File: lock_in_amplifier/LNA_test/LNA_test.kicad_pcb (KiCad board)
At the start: 2 copper layers, 110 parts, among them J1 vref-in, J10 A IN, J11 B IN, J12 POWER_IN, J15 I IN, J17 RF_Shield_One_Piece, J19 +3V3 OUT, J2 vref, J20 AMP OUT, J3 V-IN, J38 RF_Shield_One_Piece, J4 GND, J46 -5V OUT, J47 +5V OUT, J5 V+IN, J6 +5V, J7 +3V3, J8 -5V, Q1 DMN640L, Q2 DMN640L, U1 LM833, U6 lmp7721, U7 LM833, U8 AD8429

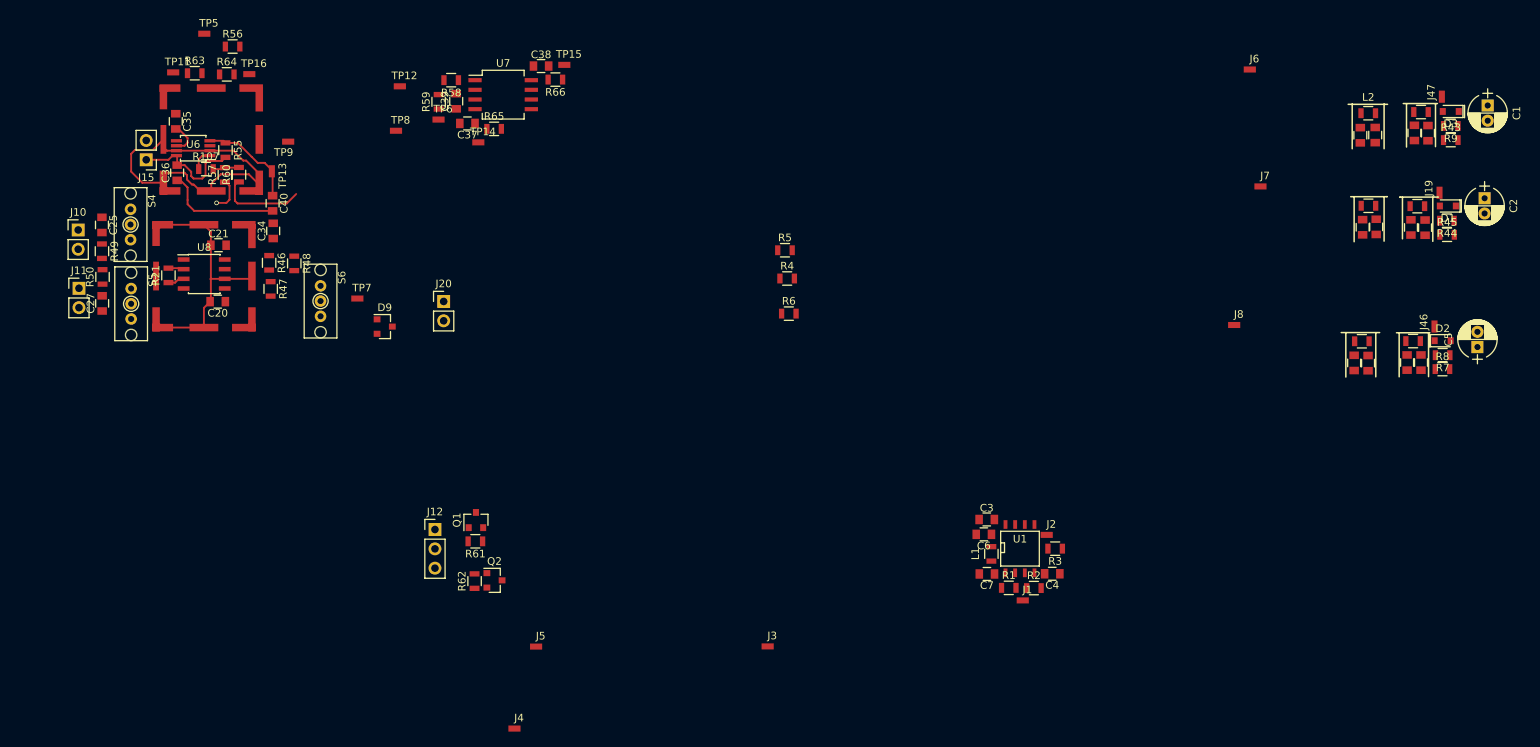
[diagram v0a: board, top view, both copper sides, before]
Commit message: initial lna and power floorplan finished.
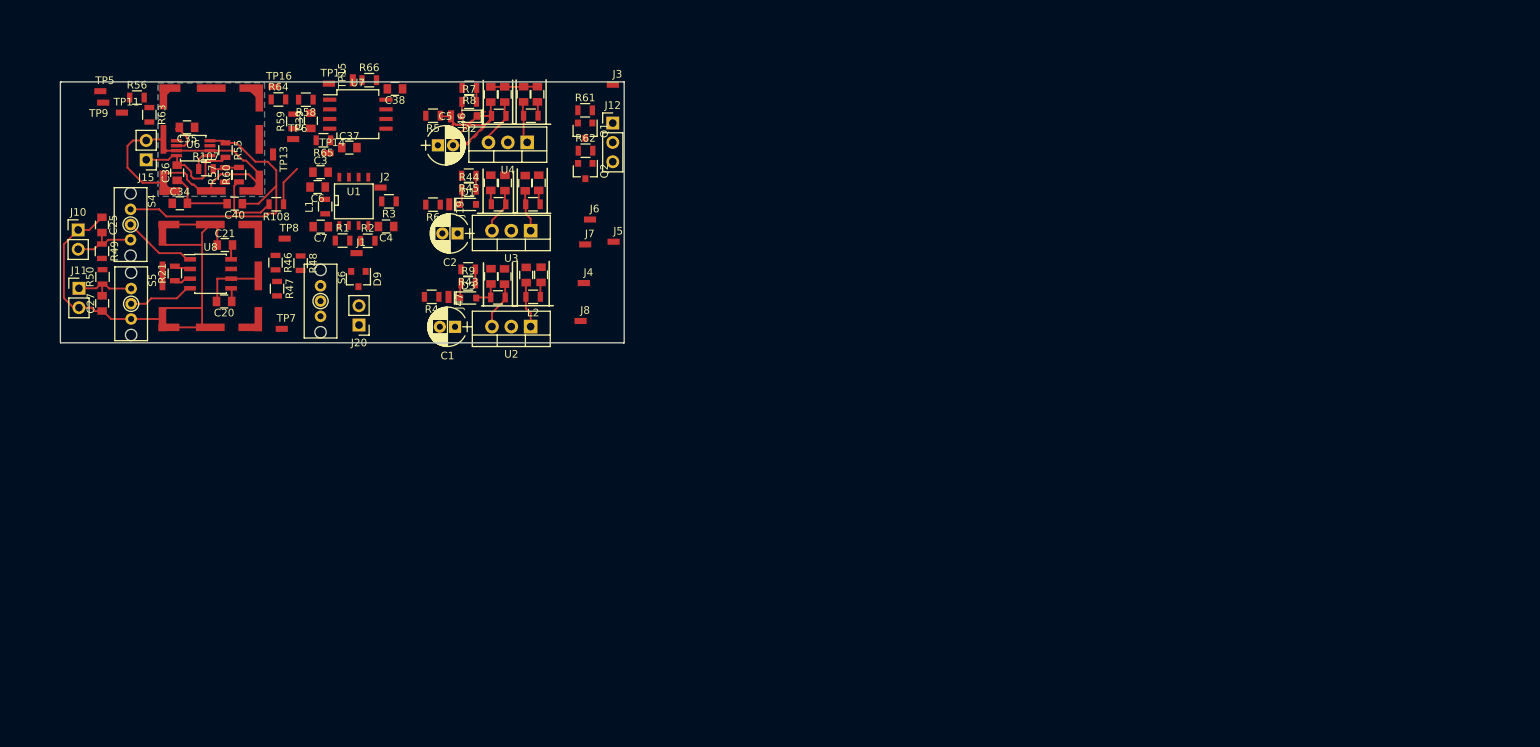
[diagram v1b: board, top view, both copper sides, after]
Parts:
- added R108: 0, Resistors_SMD:R_0805, F.Cu at (111.4, 79.3)
- added U2: lm7805, TO_SOT_Packages_THT:TO-220-3_Vertical, F.Cu at (144.8, 95.4)
- added U3: LM7833, TO_SOT_Packages_THT:TO-220-3_Vertical, F.Cu at (144.8, 82.8)
- added U4: lm7905, TO_SOT_Packages_THT:TO-220-3_Vertical, F.Cu at (144.3, 71.2)
- moved C5 139.2 mm to (132.6, 71.6), turned to 0 degrees
- moved C1 138.8 mm to (134.8, 95.4), turned to 180 degrees
- moved C2 135.1 mm to (135.2, 83.1), turned to 180 degrees
- moved R8 133.1 mm to (136.7, 64.0), turned to 180 degrees
- moved R7 132.2 mm to (136.7, 65.8), turned to 0 degrees
- moved D3 131.4 mm to (136.6, 91.6), turned to 0 degrees
- moved D2 131.3 mm to (136.7, 67.7), turned to 180 degrees
- moved R9 130.8 mm to (136.6, 89.7), turned to 0 degrees
- moved R43 130.2 mm to (136.6, 87.9), turned to 180 degrees
- moved J47 129.7 mm to (135.9, 92.1), turned to 270 degrees
- moved R45 128.8 mm to (136.7, 75.5), turned to 180 degrees
- moved D1 128.8 mm to (136.6, 79.3), turned to 0 degrees
- moved R44 128.6 mm to (136.7, 77.4), turned to 0 degrees
- moved J46 128.2 mm to (136.2, 68.4), turned to 270 degrees
- moved C17 127.2 mm to (139.5, 64.9), turned to 90 degrees
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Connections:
- J15 pad 2: GND -> /sheet5A330123/GUARD
- J17 pad 1: Net-(J17-Pad1) -> /sheet5A330123/GUARD
- Q1 pad 1: /sheet5A330121/V-_IN -> /sheet5A330121/GND_IN
- Q1 pad 2: /sheet5A330121/GND_IN -> Net-(C10-Pad1)
- Q1 pad 3: Net-(C10-Pad1) -> /sheet5A330121/V-_IN
- Q2 pad 1: /sheet5A330121/GND_IN -> /sheet5A330121/V+_IN
- Q2 pad 2: /sheet5A330121/V+_IN -> GND
- Q2 pad 3: GND -> /sheet5A330121/GND_IN
- R56 pad 1: Net-(J17-Pad1) -> /sheet5A330123/GUARD
- R58 pad 2: Net-(J17-Pad1) -> /sheet5A330123/GUARD
- R60 pad 1: Net-(R60-Pad1) -> Net-(R108-Pad2)
- TP5 pad 1: Net-(J17-Pad1) -> /sheet5A330123/GUARD
- TP8 pad 1: Net-(R60-Pad1) -> Net-(R108-Pad1)
- U6 pad 2: Net-(J17-Pad1) -> /sheet5A330123/GUARD
- U6 pad 7: Net-(J17-Pad1) -> /sheet5A330123/GUARD
- U7 pad 3: Net-(R60-Pad1) -> Net-(R108-Pad1)
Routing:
- net /sheet5A330123/GUARD: track 0.00 -> 58.8 mm
- net GND: track 38.3 -> 87.3 mm, vias 1 -> 0
- net Net-(J17-Pad1): track 47.7 -> 0.00 mm
- net -5V: track 0.00 -> 28.1 mm
- net Net-(C40-Pad1): track 13.1 -> 41.1 mm
- net Net-(R60-Pad1): track 11.5 -> 0.00 mm
- net Net-(S4-Pad2): track 0.00 -> 9.71 mm
- net Net-(R108-Pad2): track 0.00 -> 9.61 mm
- net /sheet5A330123/in-: track 0.00 -> 8.91 mm
- net /sheet5A330123/in+: track 0.00 -> 8.88 mm
- net Net-(S5-Pad2): track 0.00 -> 8.58 mm
- net Net-(C16-Pad1): track 0.00 -> 6.33 mm
- net Net-(C14-Pad1): track 0.00 -> 6.32 mm
- net Net-(C15-Pad1): track 0.00 -> 6.07 mm
- net Net-(C11-Pad1): track 0.00 -> 6.05 mm
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- added copper zone on F.Cu, net -5V
- added copper zone on B.Cu, net /sheet5A330123/GUARD
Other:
- board outline added: 74.1 x 34.3 mm
- board text added: "CAREFUL OF GROUNDING - TIA"
- board text added: "GUARD BUFFER"
- board text added: "INST AMP"
- board text added: "LNA FRONTEND"
- board text added: "PRECISION MIDPOINT"
- board text added: "PWR"
- board text added: "TIA"
- board text added: "ground plane or separate guard plane for tia?"

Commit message: initial LNA test layout
everything connected - moving towards a manufacturability test.
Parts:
- removed R64: 0, Resistors_SMD:R_0805
- removed TP16: TIAV-, footprints:tyco_RCU_0603_Probe_Pad
- removed TP9: TIA REF, footprints:tyco_RCU_0603_Probe_Pad
- moved J4 66.9 mm to (87.0, 73.4)
- moved J8 45.8 mm to (106.1, 91.9)
- moved J6 34.3 mm to (123.5, 62.2)
- moved J7 26.4 mm to (126.4, 78.7), turned to 90 degrees
- moved TP11 20.3 mm to (111.7, 62.2)
- moved R63 17.2 mm to (111.9, 66.2), turned to 0 degrees
- moved Q2 16.1 mm to (149.6, 90.8), turned to 0 degrees
- moved R62 16.1 mm to (149.6, 88.1)
- moved J5 14.3 mm to (149.8, 95.1), turned to 180 degrees
- moved TP7 14.1 mm to (126.8, 93.3), turned to 270 degrees
- moved J12 13.0 mm to (149.6, 80.2)
- moved R5 10.4 mm to (126.0, 76.2), turned to 270 degrees
- moved R58 9.24 mm to (110.8, 73.7), turned to 270 degrees
- moved J3 8.67 mm to (151.2, 68.8)
- moved TP8 8.64 mm to (116.1, 73.8)
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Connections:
- U6 pad 3: Net-(R64-Pad2) -> GND
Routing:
- net GND: track 87.3 -> 174.5 mm, vias 0 -> 46
- net +5V: track 5.68 -> 83.7 mm, vias 0 -> 2
- net -5V: track 28.1 -> 83.8 mm, vias 0 -> 2
- net /sheet5A330123/GUARD: track 58.8 -> 96.7 mm
- net +3V3: track 1.85 -> 37.0 mm
- net /sheet5A330121/V+_IN: track 3.83 -> 23.6 mm
- net /sheet5A330121/GND_IN: track 0.00 -> 17.5 mm
- net Net-(C35-Pad2): track 4.30 -> 20.8 mm
- net Net-(R46-Pad1): track 0.00 -> 13.6 mm
- net Net-(C39-Pad2): track 0.00 -> 12.7 mm
- net Net-(C7-Pad1): track 0.00 -> 12.5 mm
- net Net-(C10-Pad1): track 1.87 -> 13.9 mm
- net /sheet5A330123/amplifie_signal: track 0.00 -> 10.6 mm
- net /sheet5A330121/V-_IN: track 0.00 -> 9.93 mm
- net Net-(R46-Pad2): track 0.00 -> 8.47 mm
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- added copper zone on B.Cu, net GND
- removed copper zone on B.Cu, net /sheet5A330123/GUARD
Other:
- board size 74.1 x 34.3 mm -> 22.1 x 17.8 mm

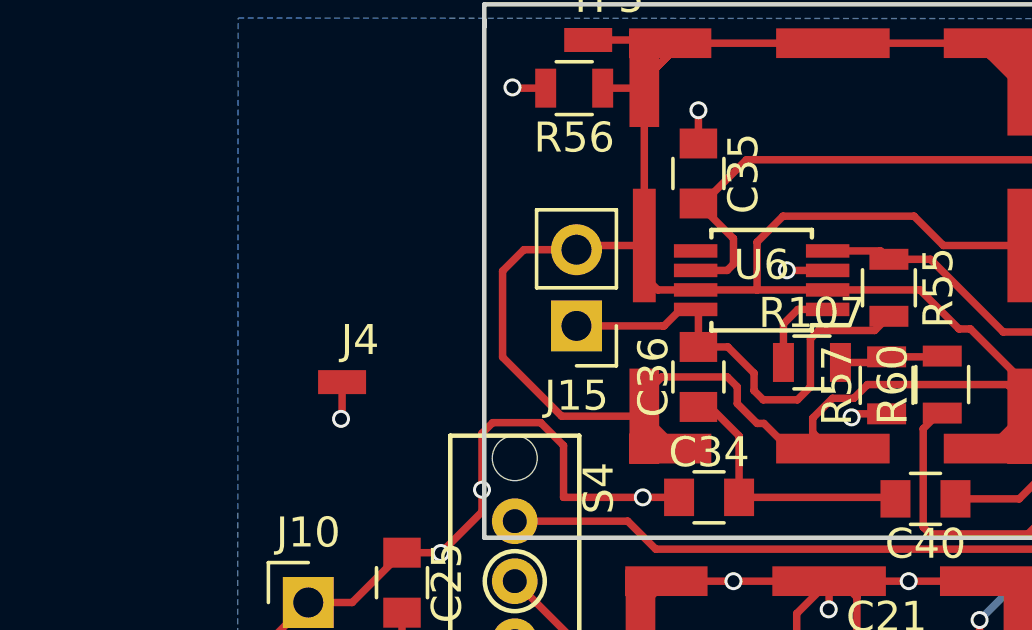
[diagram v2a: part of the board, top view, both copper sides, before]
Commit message: correct lmp7721 package - soic
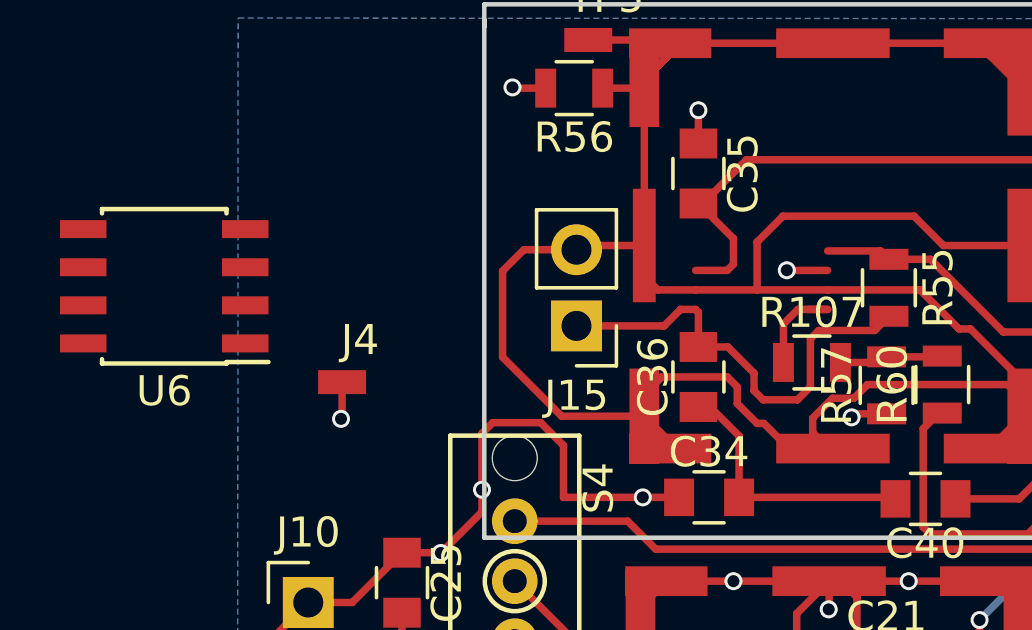
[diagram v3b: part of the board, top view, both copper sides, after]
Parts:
- U6: footprint Housings_SSOP:MSOP-8_3x3mm_Pitch0.65mm -> Housings_SOIC:SOIC-8_3.9x4.9mm_Pitch1.27mm
- moved U6 19.9 mm to (80.5, 72.1)
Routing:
- net GND: track 174.5 -> 173.1 mm, vias 46 -> 45
- net (no net): track 0.00 -> 1.36 mm, vias 0 -> 1
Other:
- board text added: "check lmp7721 package! gawd I hope I don't have to re-lay that"
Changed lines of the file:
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@@
   (general
     (links 203)
-    (no_connects 3)
+    (no_connects 10)
     (area 91.110999 62.662999 113.359001 80.593001)
     (thickness 1.6)
-    (drawings 38)
+    (drawings 39)
     (tracks 640)
     (zones 0)
@@
   (layers
     (0 F.Cu signal)
-    (31 B.Cu signal hide)
+    (31 B.Cu signal)
     (32 B.Adhes user)
     (33 F.Adhes user)
@@
     )
   )
-  (module Housings_SSOP:MSOP-8_3x3mm_Pitch0.65mm (layer F.Cu)
-    (at 100.4316 71.9328 180)
-    (descr "8-Lead Plastic Micro Small Outline Package (MS) [MSOP] (see Microchip Packaging Specification 00000049BS.pdf)")
-    (tags "SSOP 0.65")
-    (attr smd)
-    (fp_text reference U6 (at 0 0.508 180) (layer F.SilkS)
-      (effects (font (size 1 1) (thickness 0.15)))
-    )
-    (fp_text value lmp7721 (at 0 2.6 180) (layer F.Fab)
-      (effects (font (size 1 1) (thickness 0.15)))
-    )
-    (fp_line (start -0.5 -1.5) (end 1.5 -1.5) (layer F.Fab) (width 0.15))
-    (fp_line (start 1.5 -1.5) (end 1.5 1.5) (layer F.Fab) (width 0.15))
-    (fp_line (start 1.5 1.5) (end -1.5 1.5) (layer F.Fab) (width 0.15))
-    (fp_line (start -1.5 1.5) (end -1.5 -0.5) (layer F.Fab) (width 0.15))
-    (fp_line (start -1.5 -0.5) (end -0.5 -1.5) (layer F.Fab) (width 0.15))
-    (fp_line (start -3.2 -1.85) (end -3.2 1.85) (layer F.CrtYd) (width 0.05))
-    (fp_line (start 3.2 -1.85) (end 3.2 1.85) (layer F.CrtYd) (width 0.05))
-    (fp_line (start -3.2 -1.85) (end 3.2 -1.85) (layer F.CrtYd) (width 0.05))
-    (fp_line (start -3.2 1.85) (end 3.2 1.85) (layer F.CrtYd) (width 0.05))
-    (fp_line (start -1.675 -1.675) (end -1.675 -1.5) (layer F.SilkS) (width 0.15))
-    (fp_line (start 1.675 -1.675) (end 1.675 -1.425) (layer F.SilkS) (width 0.15))
-    (fp_line (start 1.675 1.675) (end 1.675 1.425) (layer F.SilkS) (width 0.15))
-    (fp_line (start -1.675 1.675) (end -1.675 1.425) (layer F.SilkS) (width 0.15))
-    (fp_line (start -1.675 -1.675) (end 1.675 -1.675) (layer F.SilkS) (width 0.15))
-    (fp_line (start -1.675 1.675) (end 1.675 1.675) (layer F.SilkS) (width 0.15))
-    (fp_line (start -1.675 -1.5) (end -2.925 -1.5) (layer F.SilkS) (width 0.15))
-    (fp_text user %R (at 0 0 180) (layer F.Fab)
-      (effects (font (size 0.6 0.6) (thickness 0.15)))
-    )
-    (pad 1 smd rect (at -2.2 -0.975 180) (size 1.45 0.45) (layers F.Cu F.Paste F.Mask)
-      (net 44 "Net-(R107-Pad1)"))
-    (pad 2 smd rect (at -2.2 -0.325 180) (size 1.45 0.45) (layers F.Cu F.Paste F.Mask)
-      (net 45 /sheet5A330123/GUARD))
-    (pad 3 smd rect (at -2.2 0.325 180) (size 1.45 0.45) (layers F.Cu F.Paste F.Mask)
-      (net 2 GND))
-    (pad 4 smd rect (at -2.2 0.975 180) (size 1.45 0.45) (layers F.Cu F.Paste F.Mask)
-      (net 24 "Net-(C40-Pad1)"))
-    (pad 5 smd rect (at 2.2 0.975 180) (size 1.45 0.45) (layers F.Cu F.Paste F.Mask)
-      (net 42 "Net-(U6-Pad5)"))
-    (pad 6 smd rect (at 2.2 0.325 180) (size 1.45 0.45) (layers F.Cu F.Paste F.Mask)
-      (net 18 "Net-(C35-Pad2)"))
-    (pad 7 smd rect (at 2.2 -0.325 180) (size 1.45 0.45) (layers F.Cu F.Paste F.Mask)
-      (net 45 /sheet5A330123/GUARD))
-    (pad 8 smd rect (at 2.2 -0.975 180) (size 1.45 0.45) (layers F.Cu F.Paste F.Mask)
-      (net 19 /sheet5A330123/I_IN))
-    (model ${KISYS3DMOD}/Housings_SSOP.3dshapes/MSOP-8_3x3mm_Pitch0.65mm.wrl
-      (at (xyz 0 0 0))
-      (scale (xyz 1 1 1))
-      (rotate (xyz 0 0 0))
-    )
-  )
   (module Resistors_SMD:R_0805 (layer F.Cu)
     (at 102.108 74.676)
@@
     )
   )
+  (module Housings_SOIC:SOIC-8_3.9x4.9mm_Pitch1.27mm (layer F.Cu)
+    (at 80.518 72.136 180)
+    (descr "8-Lead Plastic Small Outline (SN) - Narrow, 3.90 mm Body [SOIC] (see Microchip Packaging Specification 00000049BS.pdf)")
+    (tags "SOIC 1.27")
+    (attr smd)
+    (fp_text reference U6 (at 0 -3.5 180) (layer F.SilkS)
+      (effects (font (size 1 1) (thickness 0.15)))
+    )
+    (fp_text value lmp7721 (at 0 3.5 180) (layer F.Fab)
+      (effects (font (size 1 1) (thickness 0.15)))
+    )
+    (fp_text user %R (at 0 0 180) (layer F.Fab)
+      (effects (font (size 1 1) (thickness 0.15)))
+    )
+    (fp_line (start -0.95 -2.45) (end 1.95 -2.45) (layer F.Fab) (width 0.1))
+    (fp_line (start 1.95 -2.45) (end 1.95 2.45) (layer F.Fab) (width 0.1))
+    (fp_line (start 1.95 2.45) (end -1.95 2.45) (layer F.Fab) (width 0.1))
+    (fp_line (start -1.95 2.45) (end -1.95 -1.45) (layer F.Fab) (width 0.1))
+    (fp_line (start -1.95 -1.45) (end -0.95 -2.45) (layer F.Fab) (width 0.1))
+    (fp_line (start -3.73 -2.7) (end -3.73 2.7) (layer F.CrtYd) (width 0.05))
+    (fp_line (start 3.73 -2.7) (end 3.73 2.7) (layer F.CrtYd) (width 0.05))
+    (fp_line (start -3.73 -2.7) (end 3.73 -2.7) (layer F.CrtYd) (width 0.05))
+    (fp_line (start -3.73 2.7) (end 3.73 2.7) (layer F.CrtYd) (width 0.05))
+    (fp_line (start -2.075 -2.575) (end -2.075 -2.525) (layer F.SilkS) (width 0.15))
+    (fp_line (start 2.075 -2.575) (end 2.075 -2.43) (layer F.SilkS) (width 0.15))
+    (fp_line (start 2.075 2.575) (end 2.075 2.43) (layer F.SilkS) (width 0.15))
+    (fp_line (start -2.075 2.575) (end -2.075 2.43) (layer F.SilkS) (width 0.15))
+    (fp_line (start -2.075 -2.575) (end 2.075 -2.575) (layer F.SilkS) (width 0.15))
+    (fp_line (start -2.075 2.575) (end 2.075 2.575) (layer F.SilkS) (width 0.15))
+    (fp_line (start -2.075 -2.525) (end -3.475 -2.525) (layer F.SilkS) (width 0.15))
+    (pad 1 smd rect (at -2.7 -1.905 180) (size 1.55 0.6) (layers F.Cu F.Paste F.Mask)
+      (net 44 "Net-(R107-Pad1)"))
+    (pad 2 smd rect (at -2.7 -0.635 180) (size 1.55 0.6) (layers F.Cu F.Paste F.Mask)
+      (net 45 /sheet5A330123/GUARD))
+    (pad 3 smd rect (at -2.7 0.635 180) (size 1.55 0.6) (layers F.Cu F.Paste F.Mask)
+      (net 2 GND))
+    (pad 4 smd rect (at -2.7 1.905 180) (size 1.55 0.6) (layers F.Cu F.Paste F.Mask)
+      (net 24 "Net-(C40-Pad1)"))
+    (pad 5 smd rect (at 2.7 1.905 180) (size 1.55 0.6) (layers F.Cu F.Paste F.Mask)
+      (net 42 "Net-(U6-Pad5)"))
+    (pad 6 smd rect (at 2.7 0.635 180) (size 1.55 0.6) (layers F.Cu F.Paste F.Mask)
+      (net 18 "Net-(C35-Pad2)"))
+    (pad 7 smd rect (at 2.7 -0.635 180) (size 1.55 0.6) (layers F.Cu F.Paste F.Mask)
+      (net 45 /sheet5A330123/GUARD))
+    (pad 8 smd rect (at 2.7 -1.905 180) (size 1.55 0.6) (layers F.Cu F.Paste F.Mask)
+      (net 19 /sheet5A330123/I_IN))
+    (model ${KISYS3DMOD}/Housings_SOIC.3dshapes/SOIC-8_3.9x4.9mm_Pitch1.27mm.wrl
+      (at (xyz 0 0 0))
+      (scale (xyz 1 1 1))
+      (rotate (xyz 0 0 0))
+    )
+  )
+  (gr_text "check lmp7721 package! gawd I hope I don't have to re-lay that" (at 79.502 66.04) (layer Cmts.User)
+    (effects (font (size 1.5 1.5) (thickness 0.3)))
+  )
   (gr_line (start 91.186 62.738) (end 91.186 63.5) (angle 90) (layer Edge.Cuts) (width 0.15))
   (gr_line (start 113.284 62.738) (end 91.186 62.738) (angle 90) (layer Edge.Cuts) (width 0.15))
@@
   (gr_line (start 143.0274 92.6846) (end 143.0274 86.7918) (angle 90) (layer F.SilkS) (width 0.2))
   (gr_line (start 147.2184 86.7918) (end 147.2184 92.6846) (angle 90) (layer F.SilkS) (width 0.2))
+  (segment (start 102.6316 71.6078) (end 101.275 71.6078) (width 0.25) (layer F.Cu) (net 0))
+  (via (at 101.2698 71.6026) (size 0.6) (drill 0.4) (layers F.Cu B.Cu) (net 0))
+  (segment (start 101.275 71.6078) (end 101.2698 71.6026) (width 0.25) (layer F.Cu) (net 0))
   (segment (start 134.8486 95.4024) (end 134.8486 94.395) (width 0.25) (layer F.Cu) (net 1))
   (segment (start 134.8486 94.395) (end 137.6258 91.6178) (width 0.25) (layer F.Cu) (net 1))
@@
   (via (at 103.4288 76.5048) (size 0.6) (drill 0.4) (layers F.Cu B.Cu) (net 2))
   (segment (start 103.5456 76.388) (end 103.4288 76.5048) (width 0.25) (layer F.Cu) (net 2))
-  (segment (start 102.6316 71.6078) (end 101.275 71.6078) (width 0.25) (layer F.Cu) (net 2))
-  (via (at 101.2698 71.6026) (size 0.6) (drill 0.4) (layers F.Cu B.Cu) (net 2))
-  (segment (start 101.275 71.6078) (end 101.2698 71.6026) (width 0.25) (layer F.Cu) (net 2))
   (segment (start 98.3234 67.3768) (end 98.028 67.3768) (width 0.25) (layer F.Cu) (net 2))
   (segment (start 93.2332 65.532) (end 92.1512 65.532) (width 0.25) (layer F.Cu) (net 2))
@@
   (segment (start 98.3234 76.1586) (end 98.7646 76.1586) (width 0.25) (layer F.Cu) (net 17))
   (segment (start 110.9116 66.1924) (end 110.9116 67.4726) (width 0.25) (layer F.Cu) (net 18))
-  (segment (start 99.9236 67.9196) (end 98.4664 69.3768) (width 0.25) (layer F.Cu) (net 18))
-  (segment (start 110.4646 67.9196) (end 99.9236 67.9196) (width 0.25) (layer F.Cu) (net 18))
   (segment (start 110.9116 67.4726) (end 110.4646 67.9196) (width 0.25) (layer F.Cu) (net 18))
-  (segment (start 98.4664 69.3768) (end 98.3234 69.3768) (width 0.25) (layer F.Cu) (net 18))
   (segment (start 111.1092 64.1046) (end 111.1092 65.9948) (width 0.25) (layer F.Cu) (net 18))
   (segment (start 111.1092 65.9948) (end 110.9116 66.1924) (width 0.25) (layer F.Cu) (net 18))
+  (segment (start 99.9236 67.9196) (end 98.4664 69.3768) (width 0.25) (layer F.Cu) (net 18))
+  (segment (start 110.4646 67.9196) (end 99.9236 67.9196) (width 0.25) (layer F.Cu) (net 18))
+  (segment (start 98.4664 69.3768) (end 98.3234 69.3768) (width 0.25) (layer F.Cu) (net 18))
   (segment (start 98.3234 69.3768) (end 98.441 69.3768) (width 0.25) (layer F.Cu) (net 18))
   (segment (start 98.2316 71.6078) (end 99.2834 71.6078) (width 0.25) (layer F.Cu) (net 18))
